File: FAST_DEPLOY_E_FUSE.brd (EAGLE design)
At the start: 160 x 100 mm, 190 parts, among them IC1 LTC4222CUH#PBF, IC2 LTC4222CUH#PBF, IC3 ADM1177-2ARMZ-R7, IC4 ADM1177-2ARMZ-R7, IC5 MCP1792T-3302H_CB, IC6 74HC4852BQ,115, J1 JUMPERSNT-100-BK-T, J10 JUMPERSNT-100-BK-T, J11 JUMPERSNT-100-BK-T, J12 JUMPERSNT-100-BK-T, J13 JUMPERSNT-100-BK-T, J14 JUMPERSNT-100-BK-T, J15 JUMPERSNT-100-BK-T, J16 JUMPERSNT-100-BK-T, J17 JUMPERSNT-100-BK-T, J18 JUMPERSNT-100-BK-T, J19 JUMPERSNT-100-BK-T, J2 JUMPERSNT-100-BK-T, J20 JUMPERSNT-100-BK-T, J21 JUMPERSNT-100-BK-T, J22 JUMPERSNT-100-BK-T, J23 JUMPERSNT-100-BK-T, J24 JUMPERSNT-100-BK-T, J25 JUMPERSNT-100-BK-T, J26 JUMPERSNT-100-BK-T, J27 JUMPERSNT-100-BK-T, J28 JUMPERSNT-100-BK-T, J29 JUMPERSNT-100-BK-T, J3 JUMPERSNT-100-BK-T, J30 JUMPERSNT-100-BK-T, J31 JUMPERSNT-100-BK-T, J32 JUMPERSNT-100-BK-T, J4 JUMPERSNT-100-BK-T, J5 JUMPERSNT-100-BK-T, J6 JUMPERSNT-100-BK-T, J7 JUMPERSNT-100-BK-T, J8 JUMPERSNT-100-BK-T, J9 JUMPERSNT-100-BK-T, U1 SSM6N67NU,LF, U2 SSM6N67NU,LF, U3 SSM6N67NU,LF

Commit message: ~60% through layout
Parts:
- added C17: CGA5L2C0G1H104J160AA, SamacSys_Parts:CAPC3216X180N
- moved J18 273.1 mm to (144.0, 77.7)
- moved TP53 267.5 mm to (146.7, 52.2)
- moved TP54 267.5 mm to (136.5, 52.2)
- moved J17 260.2 mm to (151.2, 77.7)
- moved R49 251.8 mm to (-211.5, -26.1)
- moved R55 247.2 mm to (-204.9, -23.8)
- moved R50 242.4 mm to (-218.0, -28.3)
- moved TP43 239.7 mm to (69.3, 6.68)
- moved IC3 235.1 mm to (137.3, 65.5)
- moved IC4 235.1 mm to (118.2, 65.5)
- moved TP39 233.6 mm to (129.8, 81.5)
- moved TP40 229.1 mm to (112.9, 71.0)
- moved TP41 225.8 mm to (74.0, 7.47), turned to 90 degrees
- moved TP29 222.4 mm to (71.8, 26.5), turned to 90 degrees
- moved R14 218.6 mm to (66.3, 42.8), flipped to the bottom, turned to 270 degrees
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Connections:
- net 3.3V_LOGIC: now also C17.2, R50.1; no longer R50.2
- net GND: now also C17.1
- net SCL_0: now also R50.2; no longer R50.1
- net SDA_0: now also R46.1; no longer R44.1
- net SDA_1: now also R44.1; no longer R46.1
- net SDA_2: now also R43.1; no longer R47.1
- net SDA_3: now also R47.1; no longer R43.1
- net VSENSE_1_1: now also TP25.1
- net VSENSE_2: no longer TP25.1
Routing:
- net ADR2_0: track 0.00 -> 70.8 mm
- net SDA_1: track 0.00 -> 64.1 mm, vias 0 -> 2
- net SCL_1: track 0.00 -> 58.9 mm, vias 0 -> 4
- net ON_SIGNAL_1: track 0.00 -> 55.5 mm, vias 0 -> 2
- net ADR1_0: track 0.00 -> 54.1 mm, vias 0 -> 1
- net ADR2_1: track 0.00 -> 52.6 mm, vias 0 -> 1
- net ADR1_1: track 0.00 -> 51.6 mm, vias 0 -> 1
- net ADR0_1: track 0.00 -> 48.4 mm
- net !EN_1_0: track 0.00 -> 46.7 mm, vias 0 -> 1
- net ADR0_0: track 0.00 -> 45.9 mm
- net ON_SIGNAL_0: track 0.00 -> 45.7 mm, vias 0 -> 1
- net 3.3V_LOGIC: track 0.00 -> 43.0 mm, vias 0 -> 2
- net !EN_1_1: track 0.00 -> 41.0 mm, vias 0 -> 1
- net SDA_0: track 0.00 -> 39.1 mm, vias 0 -> 4
- net !EN_2_1: track 0.00 -> 34.9 mm, vias 0 -> 1
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
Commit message: Save before moving from 2-layer to 4-layer instead
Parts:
- moved R49 272.1 mm to (58.8, 5.64), turned to 180 degrees
- moved R36 264.7 mm to (108.6, 27.1), turned to 180 degrees
- moved R50 258.4 mm to (37.0, 13.4)
- moved R35 255.7 mm to (120.3, 27.2)
- moved R54 253.7 mm to (53.8, 6.55), turned to 180 degrees
- moved R55 245.9 mm to (37.0, 20.2), turned to 180 degrees
- moved R39 245.8 mm to (76.8, 8.08), turned to 180 degrees
- moved R47 243.5 mm to (76.9, 11.5)
- moved R58 239.6 mm to (76.8, 19.9), turned to 180 degrees
- moved R46 236.6 mm to (76.9, 9.78)
- moved R48 235.9 mm to (63.1, 5.59)
- moved R53 230.7 mm to (37.0, 10.1), turned to 180 degrees
- moved R51 230.3 mm to (50.3, 10.5), turned to 180 degrees
- moved LED12 227.2 mm to (82.7, 12.2)
- moved R52 224.8 mm to (37.0, 16.7), turned to 180 degrees
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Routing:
- net VIN_0: track 0.00 -> 147.7 mm, vias 0 -> 3
- net VIN_12V: track 0.00 -> 143.5 mm, vias 0 -> 4
- net SCL_2: track 0.00 -> 130.9 mm
- net VIN_1: track 0.00 -> 130.7 mm, vias 0 -> 1
- net SDA_2: track 0.00 -> 114.6 mm
- net ADCIN_1_0: track 0.00 -> 96.8 mm, vias 0 -> 3
- net SCL_3: track 0.00 -> 95.5 mm, vias 0 -> 4
- net SDA_3: track 0.00 -> 88.0 mm, vias 0 -> 5
- net VOUT_2_1: track 17.3 -> 90.4 mm
- net VIN_3.3V_5V: track 0.00 -> 68.8 mm, vias 0 -> 1
- net ADCIN_2_0: track 14.4 -> 73.0 mm
- net VOUT_1_1: track 16.0 -> 73.8 mm, vias 3 -> 5
- net ADCIN_1_1: track 12.6 -> 65.5 mm, vias 0 -> 2
- net ADR_0: track 0.00 -> 39.8 mm
- net ON_0: track 0.00 -> 38.9 mm, vias 0 -> 1
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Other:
- board size 160 x 100 mm -> 160.1 x 103.5 mm

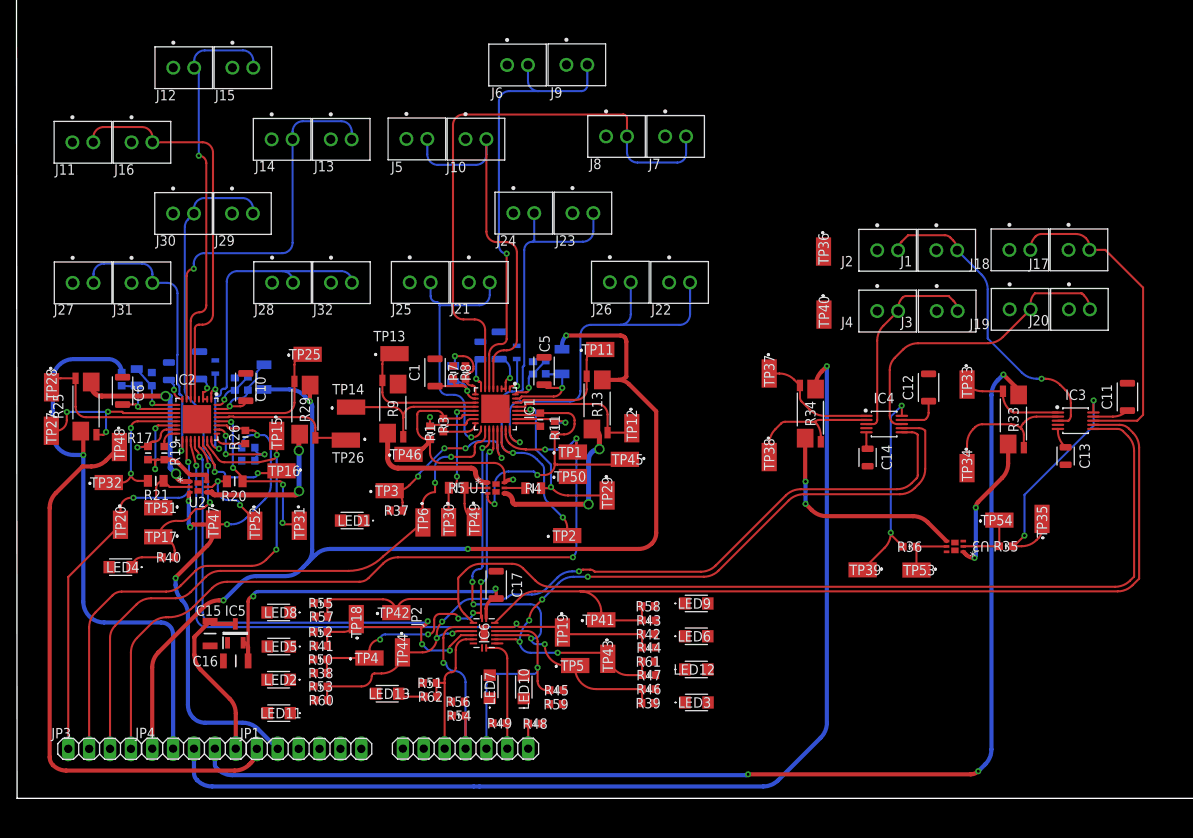
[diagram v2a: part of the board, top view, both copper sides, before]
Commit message: Began 4 layer layout
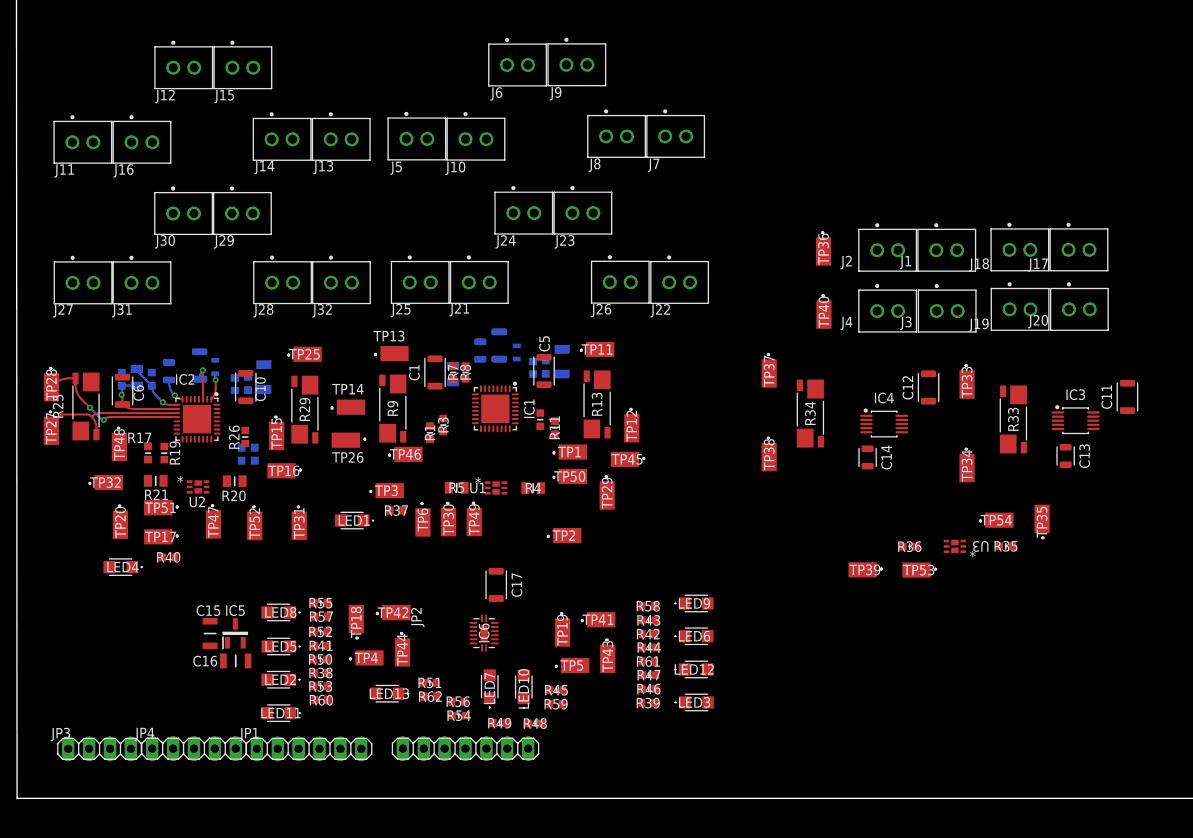
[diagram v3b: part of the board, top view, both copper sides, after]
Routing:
- net VIN_0: track 147.7 -> 0.00 mm, vias 3 -> 0
- net VIN_12V: track 143.5 -> 0.00 mm, vias 4 -> 0
- net SCL_2: track 130.9 -> 0.00 mm
- net VIN_1: track 130.7 -> 0.00 mm, vias 1 -> 0
- net SDA_2: track 114.6 -> 0.00 mm
- net ADCIN_1_0: track 96.8 -> 0.00 mm, vias 3 -> 0
- net SCL_3: track 95.5 -> 0.00 mm, vias 4 -> 0
- net VOUT_2_1: track 90.4 -> 0.00 mm, vias 2 -> 0
- net SDA_3: track 88.0 -> 0.00 mm, vias 5 -> 0
- net SDA_1: track 82.6 -> 0.00 mm, vias 2 -> 0
- net SCL_1: track 75.4 -> 0.00 mm, vias 4 -> 0
- net VOUT_1_1: track 73.8 -> 0.00 mm, vias 5 -> 0
- net ADCIN_2_0: track 73.0 -> 0.00 mm, vias 2 -> 0
- net ADR2_0: track 70.8 -> 0.00 mm
- net VIN_3.3V_5V: track 68.8 -> 0.00 mm, vias 1 -> 0
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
